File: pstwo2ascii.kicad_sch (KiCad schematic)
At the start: 34 parts, among them J1 ASCII, J2 PS2, J3 XT, J4 RS232 v24, J5 Control, J6 USB-C Power, J7 SPI, SW1 RESET, SW2 MODE, SW3 CONFIG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

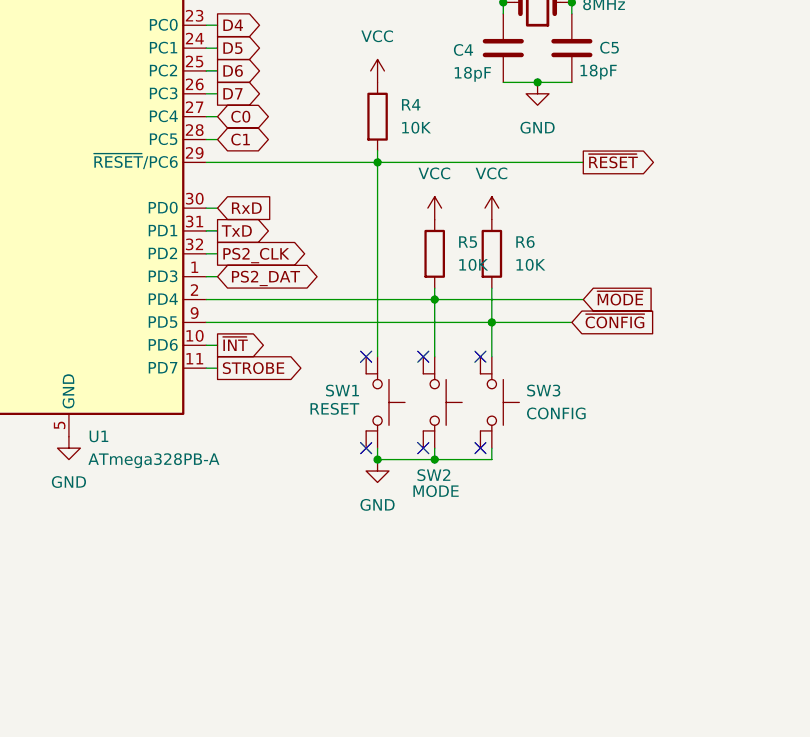
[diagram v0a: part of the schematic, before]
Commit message: Improvements. Added 3D models, changed pushbuttons to slider switches. Clearer text.
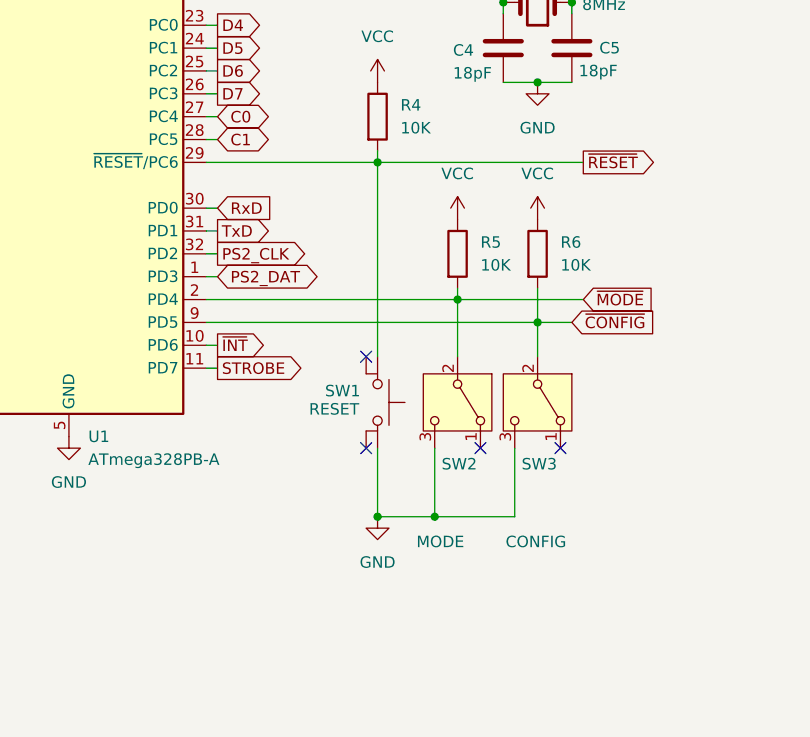
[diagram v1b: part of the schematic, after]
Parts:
- removed SW2: MODE, Sporos_Tech_Footprints:SW_SPST_Omron_B3FS-100xP_4P, symbol Sporos_Tech:SW_Push_4P
- removed SW3: CONFIG, Sporos_Tech_Footprints:SW_SPST_Omron_B3FS-100xP_4P, symbol Sporos_Tech:SW_Push_4P
- added SW2: MODE, Sporos_Tech_Footprints:CL-SB-12B-0x SPDT switch, symbol Switch:SW_SPDT
- added SW3: CONFIG, Sporos_Tech_Footprints:CL-SB-12B-0x SPDT switch, symbol Switch:SW_SPDT
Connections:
- net GND: now also SW2.3 (C), SW3.3 (C)
- net ~{CONFIG}: now also SW3.2 (B)
- net ~{MODE}: now also SW2.2 (B)
- no-connect marks 20 -> 18
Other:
- moved on the sheet: R5, R6

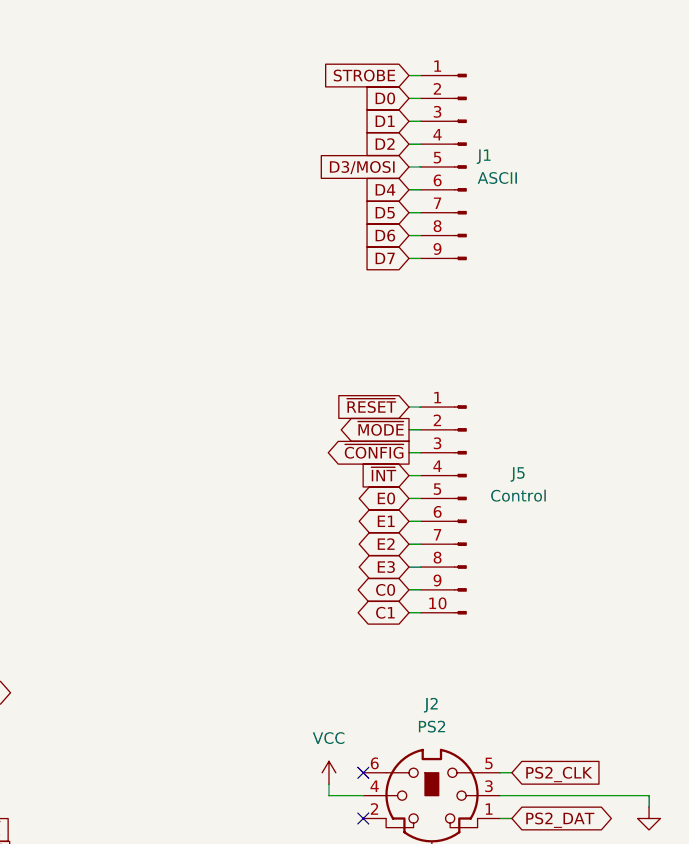
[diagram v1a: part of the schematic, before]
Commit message: Add a few extra GND pins on the pin connectors. Also added copyright information in the sheets. Also updated pretty files.
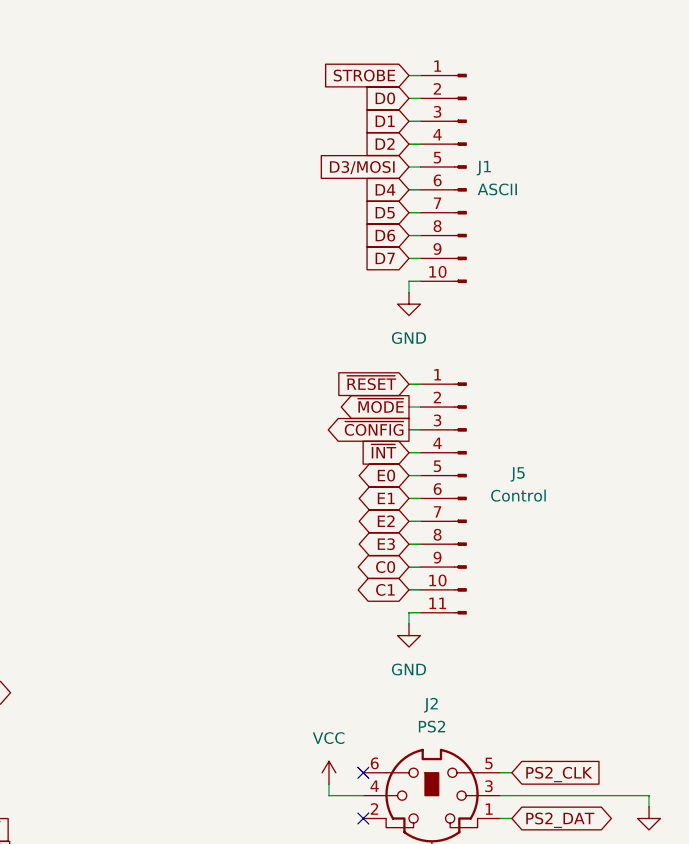
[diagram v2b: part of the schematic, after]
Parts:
- J1: footprint Connector_PinHeader_2.54mm:PinHeader_1x09_P2.54mm_Vertical -> Connector_PinHeader_2.54mm:PinHeader_1x10_P2.54mm_Vertical; symbol Connector:Conn_01x09_Pin -> Connector:Conn_01x10_Pin
- J5: footprint Connector_PinHeader_2.54mm:PinHeader_1x10_P2.54mm_Vertical -> Connector_PinHeader_2.54mm:PinHeader_1x11_P2.54mm_Vertical; symbol Connector:Conn_01x10_Pin -> Connector:Conn_01x11_Pin
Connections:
- net GND: now also J1.10 (Pin_10), J5.11 (Pin_11)
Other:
- company: Sporos Tech -> Copyright 2025, Sporos Tech, Peter de Vroomen

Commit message: Some small improvements, and assigning datasheets.
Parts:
- U1: value ATmega328PB-A -> ATmega328-AU
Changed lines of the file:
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@@
 			)
 		)
-		(property "Value" "ATmega328PB-A"
+		(property "Value" "ATmega328-AU"
 			(at 132.9533 128.27 0)
 			(effects

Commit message: Some final tweaks, changing the labels of the buttons and switches.
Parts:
- SW2: value MODE -> KBD MODE
- SW3: value CONFIG -> CONFIG MODE
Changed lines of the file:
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@@
 			)
 		)
-		(property "Datasheet" "~"
+		(property "Datasheet" "https://nl.mouser.com/datasheet/2/447/PYu_RT_1_to_0_01_RoHS_L_15-3461507.pdf"
 			(at 182.88 105.41 0)
 			(effects
@@
 			)
 		)
-		(property "Description" "Resistor"
+		(property "Description" "Resistor Yageo 0603"
 			(at 182.88 105.41 0)
 			(effects
@@
 			)
 		)
-		(property "Datasheet" "~"
+		(property "Datasheet" "https://nl.mouser.com/datasheet/2/40/TCJ-2887130.pdf"
 			(at 81.28 156.21 0)
 			(effects
@@
 			)
 		)
-		(property "Description" "Polarized capacitor"
+		(property "Description" "Tantalum capacitor 3216-18 (1206)"
 			(at 81.28 156.21 0)
 			(effects
@@
 			)
 		)
-		(property "Datasheet" "~"
+		(property "Datasheet" "https://nl.mouser.com/datasheet/2/40/TCJ-2887130.pdf"
 			(at 52.07 125.73 0)
 			(effects
@@
 			)
 		)
-		(property "Description" "Polarized capacitor"
+		(property "Description" "Tantalum capacitor 3216-18 (1206)"
 			(at 52.07 125.73 0)
 			(effects
@@
 			)
 		)
-		(property "Datasheet" "~"
+		(property "Datasheet" "https://nl.mouser.com/datasheet/2/40/TCJ-2887130.pdf"
 			(at 82.55 35.56 0)
 			(effects
@@
 			)
 		)
-		(property "Description" "Polarized capacitor"
+		(property "Description" "Tantalum capacitor 3216-18 (1206)"
 			(at 82.55 35.56 0)
 			(effects
@@
 			)
 		)
-		(property "Datasheet" "~"
+		(property "Datasheet" "https://nl.mouser.com/datasheet/2/40/TCJ-2887130.pdf"
 			(at 76.2 139.7 0)
 			(effects
@@
 			)
 		)
-		(property "Description" "Polarized capacitor"
+		(property "Description" "Tantalum capacitor 3216-18 (1206)"
 			(at 76.2 139.7 0)
 			(effects
@@
 			)
 		)
-		(property "Datasheet" "http://www.mouser.com/ds/2/18/40_c091_abd_e-75918.pdf"
+		(property "Datasheet" "https://nl.mouser.com/datasheet/2/222/KCDX-334811.pdf"
 			(at 242.57 134.62 0)
 			(effects
@@
 			)
 		)
-		(property "Description" "5-pin DIN connector (5-pin DIN-5 stereo)"
+		(property "Description" "Kycon KCDX-5S-N"
 			(at 242.57 134.62 0)
 			(effects
@@
 			)
 		)
-		(property "Datasheet" "~"
+		(property "Datasheet" "https://nl.mouser.com/datasheet/2/447/PYu_RT_1_to_0_01_RoHS_L_15-3461507.pdf"
 			(at 165.1 90.17 0)
 			(effects
@@
 			)
 		)
-		(property "Description" "Resistor"
+		(property "Description" "Resistor Yageo 0603"
 			(at 165.1 90.17 0)
 			(effects
@@
 			)
 		)
-		(property "Datasheet" "~"
+		(property "Datasheet" "https://omronfs.omron.com/en_US/ecb/products/pdf/en-b3fs.pdf"
 			(at 170.18 121.92 0)
 			(effects
@@
 			)
 		)
-		(property "Description" "Push button switch, generic, two pins"
+		(property "Description" "Omron B3FS-1000"
 			(at 161.798 121.92 0)
 			(effects
@@
 			)
 		)
-		(property "Datasheet" "~"
+		(property "Datasheet" "https://nl.mouser.com/datasheet/2/447/PYu_RT_1_to_0_01_RoHS_L_15-3461507.pdf"
 			(at 57.15 36.83 0)
 			(effects
@@
 			)
 		)
-		(property "Description" "Resistor"
+		(property "Description" "Resistor Yageo 0603"
 			(at 57.15 36.83 0)
 			(effects
@@
 			)
 		)
-		(property "Datasheet" "http://ww1.microchip.com/downloads/en/DeviceDoc/40001906C.pdf"
+		(property "Datasheet" "https://ww1.microchip.com/downloads/aemDocuments/documents/MCU08/ProductDocuments/DataSheets/ATmega48A-PA-88A-PA-168A-PA-328-P-DS-DS40002061B.pdf"
 			(at 130.81 87.63 0)
 			(effects
@@
 			)
 		)
-		(property "Description" "20MHz, 32kB Flash, 2kB SRAM, 1kB EEPROM, TQFP-32"
+		(property "Description" "ATMEGA328-AU, 20MHz, 32kB Flash, 2kB SRAM, 1kB EEPROM, TQFP-32"
 			(at 130.81 87.63 0)
 			(effects
@@
 			)
 		)
-		(property "Datasheet" "~"
+		(property "Datasheet" "https://nl.mouser.com/datasheet/2/585/MLCC-1837944.pdf"
 			(at 186.69 82.55 0)
 			(effects
@@
 			)
 		)
-		(property "Description" "Unpolarized capacitor"
+		(property "Description" "Capacitor Samsung 0603"
 			(at 186.69 82.55 0)
 			(effects
@@
 			)
 		)
-		(property "Datasheet" "~"
+		(property "Datasheet" "https://nl.mouser.com/datasheet/2/418/9/ENG_CD_146274_H3-2007782.pdf"
 			(at 114.3 163.83 0)
 			(effects
@@
 			)
 		)
-		(property "Datasheet" "~"
+		(property "Datasheet" "https://nl.mouser.com/datasheet/2/40/TCJ-2887130.pdf"
 			(at 76.2 35.56 0)
 			(effects
@@
 			)
 		)
-		(property "Description" "Polarized capacitor"
+		(property "Description" "Tantalum capacitor 3216-18 (1206)"
 			(at 76.2 35.56 0)
 			(effects
@@
 			)
 		)
-		(property "Datasheet" "~"
+		(property "Datasheet" "https://nl.mouser.com/datasheet/2/418/6/ENG_CD_146262_M_146262_2_c_dwg-2007656.pdf"
 			(at 63.5 90.17 0)
 			(effects
@@
 			)
 		)
-		(property "Datasheet" "~"
+		(property "Datasheet" "https://nl.mouser.com/datasheet/2/447/PYu_RT_1_to_0_01_RoHS_L_15-3461507.pdf"
 			(at 57.15 34.29 0)
 			(effects
@@
 			)
 		)
-		(property "Description" "Resistor"
+		(property "Description" "Resistor Yageo 0603"
 			(at 57.15 34.29 0)
 			(effects
@@
 			)
 		)
-		(property "Datasheet" "~"
+		(property "Datasheet" "https://nl.mouser.com/datasheet/2/40/TCJ-2887130.pdf"
 			(at 35.56 139.7 0)
 			(effects
@@
 			)
 		)
-		(property "Description" "Polarized capacitor"
+		(property "Description" "Tantalu capacitor 3216-18 (1206)"
 			(at 35.56 139.7 0)
 			(effects
@@
 			)
 		)
-		(property "Value" "MODE"
-			(at 169.418 137.414 90)
+		(property "Value" "KBD MODE"
+			(at 169.164 137.16 90)
 			(effects
 				(font
@@
 			)
 		)
-		(property "Datasheet" "~"
+		(property "Datasheet" "https://www.nidec-components.com/e/catalog/switch/cl-sb.pdf"
 			(at 166.37 121.92 0)
 			(effects
@@
 			)
 		)
-		(property "Description" "Switch, single pole double throw"
+		(property "Description" "Nidec CL-SB-12B-01 SPDT switch"
 			(at 173.99 121.92 0)
 			(effects
@@
 			)
 		)
-		(property "Datasheet" "~"
+		(property "Datasheet" "https://nl.mouser.com/datasheet/2/447/PYu_RT_1_to_0_01_RoHS_L_15-3461507.pdf"
 			(at 173.99 105.41 0)
 			(effects
@@
 			)
 		)
-		(property "Description" "Resistor"
+		(property "Description" "Resistor Yageo 0603"
 			(at 173.99 105.41 0)
 			(effects
@@
 			)
 		)
-		(property "Datasheet" "~"
+		(property "Datasheet" "https://nl.mouser.com/datasheet/2/3/abls-1664338.pdf"
 			(at 182.88 77.47 0)
 			(effects
@@
 			)
 		)
-		(property "Description" "Two pin crystal"
+		(property "Description" "Abracon HC/49US 8MHz, 18pF"
 			(at 182.88 77.47 0)
 			(effects
@@
 			)
 		)
-		(property "Datasheet" "~"
+		(property "Datasheet" "https://nl.mouser.com/datasheet/2/447/PYu_RT_1_to_0_01_RoHS_L_15-3461507.pdf"
 			(at 101.6 29.21 0)
 			(effects
@@
 			)
 		)
-		(property "Description" "Resistor"
+		(property "Description" "Resistor Yageo 0603"
 			(at 101.6 29.21 0)
 			(effects
@@
 			)
 		)
-		(property "Datasheet" "~"
+		(property "Datasheet" "https://nl.mouser.com/datasheet/2/585/MLCC-1837944.pdf"
 			(at 179.07 82.55 0)
 			(effects
@@
 			)
 		)
-		(property "Description" "Unpolarized capacitor"
+		(property "Description" "Capacitor Samsung 0603"
 			(at 179.07 82.55 0)
 			(effects
@@
 			)
 		)
-		(property "Value" "CONFIG"
-			(at 179.324 137.414 90)
+		(property "Value" "CONFIG MODE"
+			(at 176.53 140.462 90)
 			(effects
 				(font
@@
 			)
 		)
-		(property "Datasheet" "~"
+		(property "Datasheet" "https://www.nidec-components.com/e/catalog/switch/cl-sb.pdf"
 			(at 175.26 121.92 0)
 			(effects
@@
 			)
 		)
-		(property "Description" "Switch, single pole double throw"
+		(property "Description" "Nidec CL-SB-12B-01 SPDT switch"
 			(at 182.88 121.92 0)
 			(effects
@@
 			)
 		)
-		(property "Datasheet" "http://service.powerdynamics.com/ec/Catalog17/Section%2011.pdf"
+		(property "Datasheet" "https://nl.mouser.com/datasheet/2/222/KMDGX-334716.pdf"
 			(at 242.57 106.68 0)
 			(effects
@@
 			)
 		)
-		(property "Description" "6-pin Mini-DIN connector"
+		(property "Description" "Kycon KMDGX-6S-BS 6-pin mini DIN"
 			(at 242.57 106.68 0)
 			(effects
@@
 			)
 		)
-		(property "Datasheet" "~"
+		(property "Datasheet" "https://nl.mouser.com/datasheet/2/585/MLCC-1837944.pdf"
 			(at 125.73 44.45 0)
 			(effects
@@
 			)
 		)
-		(property "Description" "Unpolarized capacitor"
+		(property "Description" "Capacitor Samsung MLCC 0603"
 			(at 125.73 44.45 0)
 			(effects
@@
 			)
 		)
-		(property "Datasheet" "https://www.usb.org/sites/default/files/documents/usb_type-c.zip"
+		(property "Datasheet" "https://www.molex.com/en-us/products/part-detail-pdf/2137160001?display=pdf"
 			(at 40.64 44.45 0)
 			(effects
@@
 			)
 		)
-		(property "Description" "USB 2.0-only 16P Type-C Receptacle connector"
+		(property "Description" "Molex 213617-001 USB-C 16-pin"
 			(at 36.83 44.45 0)
 			(effects
@@
 			)
 		)
-		(property "Datasheet" "~"
+		(property "Datasheet" "https://nl.mouser.com/datasheet/2/40/TCJ-2887130.pdf"
 			(at 81.28 148.59 0)
 			(effects
@@
 			)
 		)
-		(property "Description" "Polarized capacitor"
+		(property "Description" "Tantalum capacitor 3216-18 (1206)"
 			(at 81.28 148.59 0)
 			(effects
@@
 			)
 		)
-		(property "Datasheet" "~"
+		(property "Datasheet" "https://nl.mouser.com/datasheet/2/418/9/ENG_CD_146274_H3-2007782.pdf"
 			(at 246.38 36.83 0)
 			(effects
@@
 			)
 		)
-		(property "Datasheet" "~"
+		(property "Datasheet" "https://nl.mouser.com/datasheet/2/418/9/ENG_CD_146274_H3-2007782.pdf"
 			(at 246.38 73.66 0)
 			(effects
